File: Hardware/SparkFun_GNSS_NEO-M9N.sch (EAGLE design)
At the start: 55 parts, among them J1 MICROMOD_STANDARD, J4 Bus Selection, U1 U-BLOX_NEO-M9N, U2 3.3V, U3 EEPROM, U4 74HC1G04

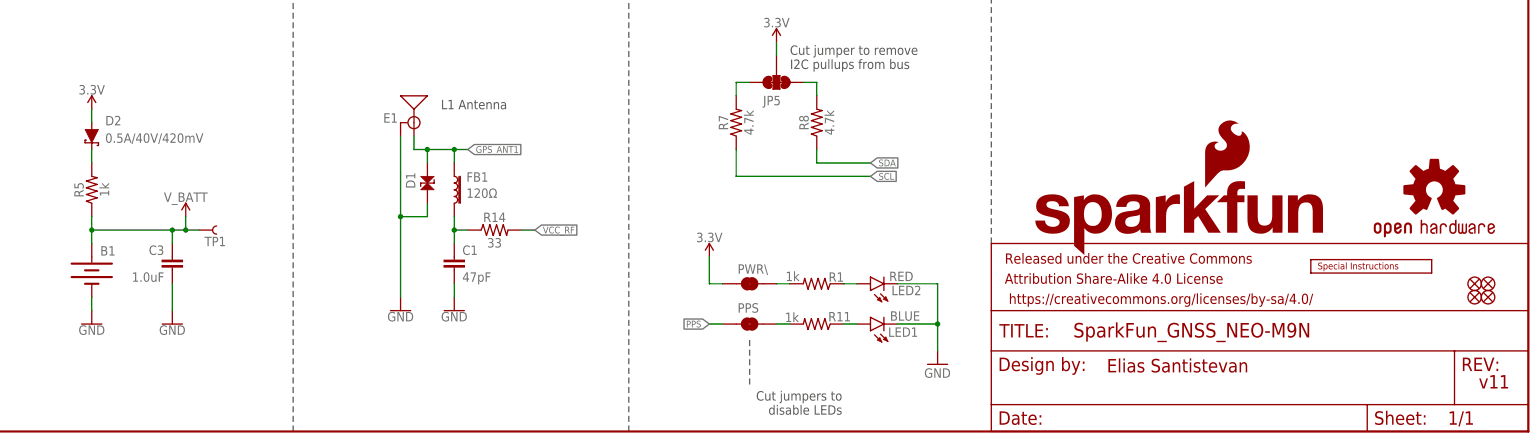
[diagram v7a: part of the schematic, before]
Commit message: Replaces SMA connector with u.FL
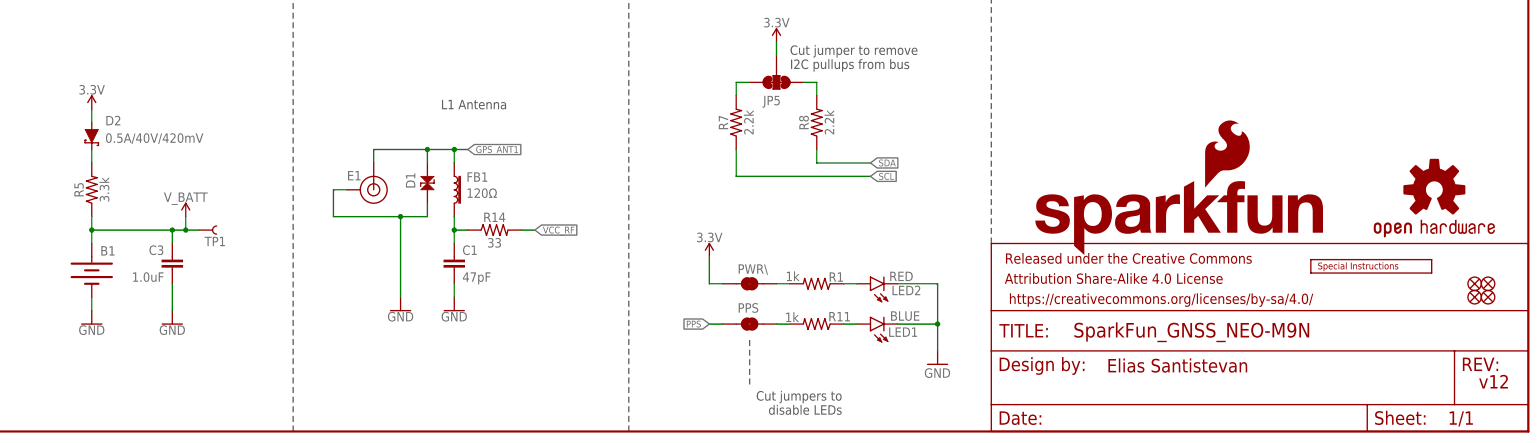
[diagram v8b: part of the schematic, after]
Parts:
- E1: value ANTENNA-SMA-GROUNDEDEDGE_SMA_THIN -> U.FL; device SparkFun-RF:ANTENNA-SMA-GROUNDEDEDGE_SMA_THIN -> SparkFun-Connectors:U.FL2PIN
- R5: value 1k -> 3.3k; device SparkFun-Resistors:1KOHM-0603-1/10W-1% -> SparkFun-Resistors:3.3KOHM-0603-1/10W-1%
- R7, R8: value 4.7k -> 2.2k; device SparkFun-Resistors:4.7KOHM-0603-1/10W-1% -> SparkFun-Resistors:2.2KOHM-0603-1/10W-1%
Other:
- note added: "v12"
- note removed: "v11"
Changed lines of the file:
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@@
 <part name="GND5" library="SparkFun-PowerSymbols" deviceset="GND" device=""/>
 <part name="GND10" library="SparkFun-PowerSymbols" deviceset="GND" device=""/>
-<part name="R7" library="SparkFun-Resistors" deviceset="4.7KOHM" device="-0603-1/10W-1%" value="4.7k"/>
-<part name="R8" library="SparkFun-Resistors" deviceset="4.7KOHM" device="-0603-1/10W-1%" value="4.7k"/>
+<part name="R7" library="SparkFun-Resistors" deviceset="2.2KOHM" device="-0603-1/10W-1%" value="2.2k"/>
+<part name="R8" library="SparkFun-Resistors" deviceset="2.2KOHM" device="-0603-1/10W-1%" value="2.2k"/>
 <part name="JP5" library="SparkFun-Jumpers" deviceset="JUMPER-SMT_3_2-NC_TRACE" device="_SILK" package3d_urn="urn:adsk.eagle:package:39289/1" value="JUMPER-SMT_3_2-NC_TRACE_SILK"/>
 <part name="SUPPLY9" library="SparkFun-PowerSymbols" deviceset="3.3V" device=""/>
@@
 <part name="D2" library="SparkFun-DiscreteSemi" deviceset="DIODE-SCHOTTKY" device="-PMEG4005EJ" value="0.5A/40V/420mV"/>
 <part name="SUPPLY5" library="SparkFun-PowerSymbols" deviceset="3.3V" device=""/>
-<part name="R5" library="SparkFun-Resistors" deviceset="1KOHM" device="-0603-1/10W-1%" value="1k"/>
+<part name="R5" library="SparkFun-Resistors" deviceset="3.3KOHM" device="-0603-1/10W-1%" value="3.3k"/>
 <part name="R11" library="SparkFun-Resistors" deviceset="1KOHM" device="-0603-1/10W-1%" value="1k"/>
 <part name="SUPPLY1" library="SparkFun-PowerSymbols" deviceset="3.3V" device=""/>
@@
 <part name="GND17" library="SparkFun-PowerSymbols" deviceset="GND" device=""/>
 <part name="SUPPLY12" library="SparkFun-PowerSymbols" deviceset="3.3V" device=""/>
-<part name="E1" library="SparkFun-RF" deviceset="ANTENNA-SMA-GROUNDED" device="EDGE_SMA_THIN" value="ANTENNA-SMA-GROUNDEDEDGE_SMA_THIN"/>
+<part name="E1" library="SparkFun-Connectors" deviceset="U.FL2PIN" device="" value="U.FL"/>
 <part name="FB1" library="SparkFun-Coils" deviceset="FERRITE_BEAD-120_OHM" device="-0402" value="120Ω"/>
 <part name="C1" library="SparkFun-Capacitors" deviceset="47PF" device="-0402-25V-5%-X7R" value="47pF"/>
@@
 <sheet>
 <plain>
-<text x="422.402" y="8.128" size="2.54" layer="94" font="vector">v11</text>
+<text x="422.402" y="8.128" size="2.54" layer="94" font="vector">v12</text>
 <text x="71.12" y="182.88" size="1.778" layer="97" font="vector" align="center">7-bit unshifted I2C address: 0x42</text>
 <text x="292.1" y="68.58" size="1.778" layer="97" font="vector">Cut jumper to remove
@@
 <attribute name="VALUE" x="276.86" y="35.814" size="1.778" layer="96" font="vector" align="bottom-center"/>
 </instance>
-<instance part="E1" gate="G$1" x="220.98" y="58.42" smashed="yes" rot="MR0">
-<attribute name="NAME" x="217.932" y="58.42" size="1.778" layer="95" font="vector" rot="MR0"/>
+<instance part="E1" gate="G$1" x="213.36" y="45.72" smashed="yes" rot="MR90">
+<attribute name="NAME" x="211.074" y="47.498" size="1.778" layer="95" font="vector" rot="MR0"/>
 </instance>
 <instance part="FB1" gate="G$1" x="228.6" y="45.72" smashed="yes">
@@
 <segment>
 <pinref part="GND27" gate="1" pin="GND"/>
-<pinref part="E1" gate="G$1" pin="GND"/>
-<wire x1="218.44" y1="55.88" x2="218.44" y2="40.64" width="0.1524" layer="91"/>
 <pinref part="D1" gate="D1" pin="1"/>
 <wire x1="218.44" y1="40.64" x2="218.44" y2="25.4" width="0.1524" layer="91"/>
 <wire x1="223.52" y1="43.18" x2="223.52" y2="40.64" width="0.1524" layer="91"/>
 <wire x1="223.52" y1="40.64" x2="218.44" y2="40.64" width="0.1524" layer="91"/>
+<wire x1="218.44" y1="40.64" x2="205.74" y2="40.64" width="0.1524" layer="91"/>
 <junction x="218.44" y="40.64"/>
+<wire x1="205.74" y1="40.64" x2="205.74" y2="45.72" width="0.1524" layer="91"/>
+<pinref part="E1" gate="G$1" pin="GND"/>
+<wire x1="205.74" y1="45.72" x2="208.28" y2="45.72" width="0.1524" layer="91"/>
 </segment>
 <segment>
@@
 <label x="231.14" y="53.34" size="1.27" layer="95" xref="yes"/>
 <pinref part="E1" gate="G$1" pin="SIGNAL"/>
-<wire x1="220.98" y1="55.88" x2="220.98" y2="53.34" width="0.1524" layer="91"/>
-<wire x1="220.98" y1="53.34" x2="223.52" y2="53.34" width="0.1524" layer="91"/>
+<wire x1="213.36" y1="50.8" x2="213.36" y2="53.34" width="0.1524" layer="91"/>
+<wire x1="213.36" y1="53.34" x2="223.52" y2="53.34" width="0.1524" layer="91"/>
 <pinref part="FB1" gate="G$1" pin="1"/>
 <wire x1="223.52" y1="53.34" x2="228.6" y2="53.34" width="0.1524" layer="91"/>
